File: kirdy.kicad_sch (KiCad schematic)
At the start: 0 parts

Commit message: add driver stage sch
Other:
- added sheet driveStage (driveStage.kicad_sch)
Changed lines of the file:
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@@
 (kicad_sch (version 20211123) (generator eeschema)
   (paper "A3")
-  (symbol_instances)
+  (sheet (at 270.51 93.98) (size 25.4 19.05) (fields_autoplaced)
+    (stroke (width 0.1524) (type solid) (color 0 0 0 0))
+    (fill (color 0 0 0 0.0000))
+    (property "Sheet name" "driveStage" (id 0) (at 270.51 93.2684 0)
+      (effects (font (size 1.27 1.27)) (justify left bottom))
+    )
+    (property "Sheet file" "driveStage.kicad_sch" (id 1) (at 270.51 113.6146 0)
+      (effects (font (size 1.27 1.27)) (justify left top))
+    )
+    (pin "GND_SEN" output (at 270.51 106.68 180)
+      (effects (font (size 1.27 1.27)) (justify left))
+    )
+    (pin "LD-" output (at 295.91 106.68 0)
+      (effects (font (size 1.27 1.27)) (justify right))
+    )
+    (pin "LD+" output (at 295.91 100.33 0)
+      (effects (font (size 1.27 1.27)) (justify right))
+    )
+    (pin "LD_DAC" input (at 270.51 100.33 180)
+      (effects (font (size 1.27 1.27)) (justify left))
+    )
+  )
+  (sheet_instances
+    (path "/" (page "1"))
+    (path "/7fc2620b-bac4-49c0-a276-7d2a46898037" (page "2"))
+  )
+  (symbol_instances
+    (path "/7fc2620b-bac4-49c0-a276-7d2a46898037/7f2ae8de-9741-4de8-8b3e-0cbf1d496d0b"
+      (reference "#PWR?") (unit 1) (value "GND") (footprint "")
+    )
+    (path "/7fc2620b-bac4-49c0-a276-7d2a46898037/89be3b87-0315-4e54-b96d-03ea2414961f"
+      (reference "#PWR?") (unit 1) (value "+9VA") (footprint "")
+    )
+    (path "/7fc2620b-bac4-49c0-a276-7d2a46898037/9119661d-44f6-446a-9801-ce7bdada5f6c"
+      (reference "#PWR?") (unit 1) (value "-6V") (footprint "")
+    )
+    (path "/7fc2620b-bac4-49c0-a276-7d2a46898037/91ab56d9-20e0-4249-9981-a5a11df12169"
+      (reference "#PWR?") (unit 1) (value "GND") (footprint "")
+    )
+    (path "/7fc2620b-bac4-49c0-a276-7d2a46898037/94d8c0ef-788e-401d-b84d-b1e1c20b5ad0"
+      (reference "#PWR?") (unit 1) (value "+15V") (footprint "")
+    )
+    (path "/7fc2620b-bac4-49c0-a276-7d2a46898037/b5336e6d-b40e-4302-8070-a2e20e788664"
+      (reference "#PWR?") (unit 1) (value "GND") (footprint "")
+    )
+    (path "/7fc2620b-bac4-49c0-a276-7d2a46898037/b9da8ef3-8685-462f-8a3e-c3779610dd6e"
+      (reference "#PWR?") (unit 1) (value "+9VA") (footprint "")
+    )
+    (path "/7fc2620b-bac4-49c0-a276-7d2a46898037/bcbda3c7-7e9b-441d-b86c-cb49c070efc8"
+      (reference "#PWR?") (unit 1) (value "GND") (footprint "")
+    )
+    (path "/7fc2620b-bac4-49c0-a276-7d2a46898037/c66bdd89-bde9-4c51-94d1-a5152521e393"
+      (reference "#PWR?") (unit 1) (value "+8V") (footprint "")
+    )
+    (path "/7fc2620b-bac4-49c0-a276-7d2a46898037/cc384f65-7f0d-4678-98b8-ac73a44b359a"
+      (reference "#PWR?") (unit 1) (value "-6V") (footprint "")
+    )
+    (path "/7fc2620b-bac4-49c0-a276-7d2a46898037/cee05324-592d-4982-97cf-77964e04d4ac"
+      (reference "#PWR?") (unit 1) (value "GND") (footprint "")
+    )
+    (path "/7fc2620b-bac4-49c0-a276-7d2a46898037/d79107b5-7dc2-415e-945e-ed09fd9cfe77"
+      (reference "#PWR?") (unit 1) (value "-6V") (footprint "")
+    )
+    (path "/7fc2620b-bac4-49c0-a276-7d2a46898037/e25c6fe0-b2f1-40d9-ac68-8d2d96853d01"
+      (reference "#PWR?") (unit 1) (value "+9VA") (footprint "")
+    )
+    (path "/7fc2620b-bac4-49c0-a276-7d2a46898037/e42d3e8b-b42d-4358-a3c4-e0df9650fb31"
+      (reference "#PWR?") (unit 1) (value "+9VA") (footprint "")
+    )
+    (path "/7fc2620b-bac4-49c0-a276-7d2a46898037/f4f71da4-602f-4bb4-aa0d-484f08abc473"
+      (reference "#PWR?") (unit 1) (value "+15V") (footprint "")
+    )
+    (path "/7fc2620b-bac4-49c0-a276-7d2a46898037/220f7c28-69b1-42e7-83ce-7bb31e5cf05d"
+      (reference "C?") (unit 1) (value "2u") (footprint "")
+    )
+    (path "/7fc2620b-bac4-49c0-a276-7d2a46898037/474c426e-35aa-4bc8-ac82-e7acb6bf064c"
+      (reference "C?") (unit 1) (value "10n") (footprint "")
+    )
+    (path "/7fc2620b-bac4-49c0-a276-7d2a46898037/e8a7395c-b328-4a48-81a4-7da6a4753156"
+      (reference "C?") (unit 1) (value "2u") (footprint "")
+    )
+    (path "/7fc2620b-bac4-49c0-a276-7d2a46898037/e2529b99-2d1f-424b-948b-cb83b5441da0"
+      (reference "D?") (unit 1) (value "AQ4020-01FTG-C") (footprint "")
+    )
+    (path "/7fc2620b-bac4-49c0-a276-7d2a46898037/fc3e1e88-39dd-4e44-9550-0de98037638f"
+      (reference "J?") (unit 1) (value "MOD_IN") (footprint "")
+    )
+    (path "/7fc2620b-bac4-49c0-a276-7d2a46898037/d481456c-376e-4c18-aab0-143380a08806"
+      (reference "Q?") (unit 1) (value "CSD17507Q5A") (footprint "Package_TO_SOT_SMD:TDSON-8-1")
+    )
+    (path "/7fc2620b-bac4-49c0-a276-7d2a46898037/066d5892-5cd5-4bea-b526-a87f3a5c11e8"
+      (reference "R?") (unit 1) (value "100") (footprint "")
+    )
+    (path "/7fc2620b-bac4-49c0-a276-7d2a46898037/3ee38521-8197-424b-afd0-d940f0fbf437"
+      (reference "R?") (unit 1) (value "100") (footprint "")
+    )
+    (path "/7fc2620b-bac4-49c0-a276-7d2a46898037/4f339c66-c682-43a9-8f4e-7ad41804bdc2"
+      (reference "R?") (unit 1) (value "300") (footprint "")
+    )
+    (path "/7fc2620b-bac4-49c0-a276-7d2a46898037/84d1caf1-6f0d-4adb-bda1-ca435ebeff03"
+      (reference "R?") (unit 1) (value "2k") (footprint "")
+    )
+    (path "/7fc2620b-bac4-49c0-a276-7d2a46898037/89ee40b5-e3cd-44df-ab7b-4cda054672f5"
+      (reference "R?") (unit 1) (value "R_Shunt") (footprint "")
+    )
+    (path "/7fc2620b-bac4-49c0-a276-7d2a46898037/affb61ec-84ab-440d-a648-f96126f479ed"
+      (reference "R?") (unit 1) (value "100") (footprint "")
+    )
+    (path "/7fc2620b-bac4-49c0-a276-7d2a46898037/b3c70cb7-9c59-476f-852d-2641f246969d"
+      (reference "R?") (unit 1) (value "50") (footprint "")
+    )
+    (path "/7fc2620b-bac4-49c0-a276-7d2a46898037/b999677c-fac2-421c-937e-afea837078d3"
+      (reference "R?") (unit 1) (value "100") (footprint "")
+    )
+    (path "/7fc2620b-bac4-49c0-a276-7d2a46898037/c5994ec4-b59b-4eb4-8847-d4ef36a60a0c"
+      (reference "R?") (unit 1) (value "1") (footprint "")
+    )
+    (path "/7fc2620b-bac4-49c0-a276-7d2a46898037/df19f4dc-6f09-439e-a4b3-58fc0b6e1223"
+      (reference "R?") (unit 1) (value "10") (footprint "")
+    )
+    (path "/7fc2620b-bac4-49c0-a276-7d2a46898037/6f857960-a9ff-452e-bba2-080502805e7a"
+      (reference "SW?") (unit 1) (value "SW_DIP_x03") (footprint "")
+    )
+    (path "/7fc2620b-bac4-49c0-a276-7d2a46898037/4553d9ae-3656-48c1-ba42-349c8ea6d675"
+      (reference "U?") (unit 1) (value "ADA4898-1YRDZ") (footprint "Package_SO:SOIC-8-1EP_3.9x4.9mm_P1.27mm_EP2.29x3mm")
+    )
+    (path "/7fc2620b-bac4-49c0-a276-7d2a46898037/75ce4c72-4d1d-4fd1-a700-9ce5fb7cb68a"
+      (reference "U?") (unit 1) (value "ADA4898-1YRDZ") (footprint "Package_SO:SOIC-8-1EP_3.9x4.9mm_P1.27mm_EP2.29x3mm")
+    )
+    (path "/7fc2620b-bac4-49c0-a276-7d2a46898037/cab8be84-b688-4aaa-b54c-d8be85dc55c5"
+      (reference "U?") (unit 1) (value "ADA4898-1YRDZ") (footprint "Package_SO:SOIC-8-1EP_3.9x4.9mm_P1.27mm_EP2.29x3mm")
+    )
+  )
 )

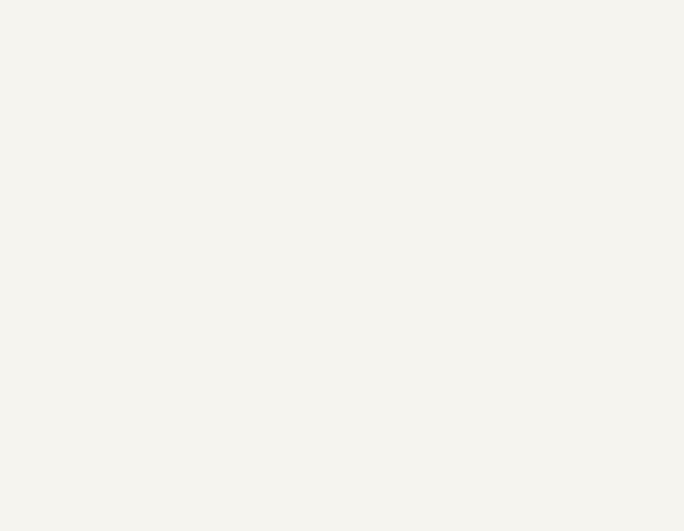
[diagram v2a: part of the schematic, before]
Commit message: add ref dac
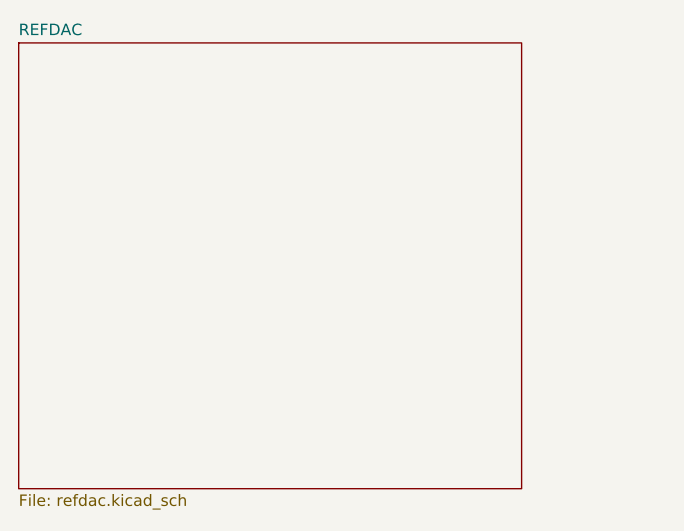
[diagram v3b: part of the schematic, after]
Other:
- added sheet REFDAC (refdac.kicad_sch)
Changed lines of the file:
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@@
 (kicad_sch (version 20211123) (generator eeschema)
   (paper "A3")
+  (sheet (at 173.99 91.44) (size 55.88 49.53) (fields_autoplaced)
+    (stroke (width 0.1524) (type solid) (color 0 0 0 0))
+    (fill (color 0 0 0 0.0000))
+    (property "Sheet name" "REFDAC" (id 0) (at 173.99 90.7284 0)
+      (effects (font (size 1.27 1.27)) (justify left bottom))
+    )
+    (property "Sheet file" "refdac.kicad_sch" (id 1) (at 173.99 141.5546 0)
+      (effects (font (size 1.27 1.27)) (justify left top))
+    )
+  )
   (sheet (at 270.51 93.98) (size 25.4 19.05) (fields_autoplaced)
     (stroke (width 0.1524) (type solid) (color 0 0 0 0))
@@
     (path "/" (page "1"))
     (path "/7fc2620b-bac4-49c0-a276-7d2a46898037" (page "2"))
+    (path "/5c501399-91aa-4646-9dc0-aa6b782690af" (page "3"))
   )
   (symbol_instances
+    (path "/7fc2620b-bac4-49c0-a276-7d2a46898037/22dd391c-8e48-413f-8e44-9f72eefb4601"
+      (reference "#PWR?") (unit 1) (value "+15V") (footprint "")
+    )
+    (path "/7fc2620b-bac4-49c0-a276-7d2a46898037/234258fd-ca43-4b0f-bd3b-37a0c1d653dc"
+      (reference "#PWR?") (unit 1) (value "+9VA") (footprint "")
+    )
+    (path "/7fc2620b-bac4-49c0-a276-7d2a46898037/30c37857-bcd7-4d18-b782-dd4e651118cd"
+      (reference "#PWR?") (unit 1) (value "-6V") (footprint "")
+    )
+    (path "/7fc2620b-bac4-49c0-a276-7d2a46898037/42e81420-64c1-4191-91f2-d9ce2b7f0c58"
+      (reference "#PWR?") (unit 1) (value "GND") (footprint "")
+    )
+    (path "/7fc2620b-bac4-49c0-a276-7d2a46898037/5f796a2f-98e9-46e3-a254-aaf7ea8e8609"
+      (reference "#PWR?") (unit 1) (value "+9VA") (footprint "")
+    )
+    (path "/7fc2620b-bac4-49c0-a276-7d2a46898037/692ead24-1a3f-435a-8011-daf8f013e94d"
+      (reference "#PWR?") (unit 1) (value "-6V") (footprint "")
+    )
+    (path "/7fc2620b-bac4-49c0-a276-7d2a46898037/799206b5-376e-4365-9dbe-4ba1050c7f50"
+      (reference "#PWR?") (unit 1) (value "GND") (footprint "")
+    )
     (path "/7fc2620b-bac4-49c0-a276-7d2a46898037/7f2ae8de-9741-4de8-8b3e-0cbf1d496d0b"
       (reference "#PWR?") (unit 1) (value "GND") (footprint "")
@@
       (reference "#PWR?") (unit 1) (value "+15V") (footprint "")
     )
+    (path "/7fc2620b-bac4-49c0-a276-7d2a46898037/95044b80-4a7b-44f0-ba10-b3f8d39e8d8b"
+      (reference "#PWR?") (unit 1) (value "GND") (footprint "")
+    )
     (path "/7fc2620b-bac4-49c0-a276-7d2a46898037/b5336e6d-b40e-4302-8070-a2e20e788664"
       (reference "#PWR?") (unit 1) (value "GND") (footprint "")
@@
       (reference "#PWR?") (unit 1) (value "-6V") (footprint "")
     )
+    (path "/7fc2620b-bac4-49c0-a276-7d2a46898037/e03d4cfa-81b2-4add-b063-90058145447f"
+      (reference "#PWR?") (unit 1) (value "-6V") (footprint "")
+    )
     (path "/7fc2620b-bac4-49c0-a276-7d2a46898037/e25c6fe0-b2f1-40d9-ac68-8d2d96853d01"
       (reference "#PWR?") (unit 1) (value "+9VA") (footprint "")
@@
       (reference "C?") (unit 1) (value "2u") (footprint "")
     )
+    (path "/7fc2620b-bac4-49c0-a276-7d2a46898037/39400eb9-6410-4341-8c26-1e54fd41195f"
+      (reference "C?") (unit 1) (value "10u") (footprint "")
+    )
     (path "/7fc2620b-bac4-49c0-a276-7d2a46898037/474c426e-35aa-4bc8-ac82-e7acb6bf064c"
       (reference "C?") (unit 1) (value "10n") (footprint "")
     )
+    (path "/7fc2620b-bac4-49c0-a276-7d2a46898037/6515a0cc-09fd-42e3-8559-ed97c2e10919"
+      (reference "C?") (unit 1) (value "100n") (footprint "")
+    )
+    (path "/7fc2620b-bac4-49c0-a276-7d2a46898037/7d6a0bc2-603a-43a2-992b-4f35cbb0a1f8"
+      (reference "C?") (unit 1) (value "100n") (footprint "")
+    )
+    (path "/7fc2620b-bac4-49c0-a276-7d2a46898037/9e5b3b75-838d-49ca-9d77-cb76ab7d1e4e"
+      (reference "C?") (unit 1) (value "10u") (footprint "")
+    )
+    (path "/7fc2620b-bac4-49c0-a276-7d2a46898037/cf733f3d-f3a4-44f4-a550-52da39242bf1"
+      (reference "C?") (unit 1) (value "100n") (footprint "")
+    )
+    (path "/7fc2620b-bac4-49c0-a276-7d2a46898037/e436bca2-7176-45a0-a972-406de4b69486"
+      (reference "C?") (unit 1) (value "100n") (footprint "")
+    )
     (path "/7fc2620b-bac4-49c0-a276-7d2a46898037/e8a7395c-b328-4a48-81a4-7da6a4753156"
       (reference "C?") (unit 1) (value "2u") (footprint "")
     )
+    (path "/7fc2620b-bac4-49c0-a276-7d2a46898037/f89d2343-5bb4-4a92-9abf-ee1606dfe7e0"
+      (reference "C?") (unit 1) (value "100n") (footprint "")
+    )
+    (path "/7fc2620b-bac4-49c0-a276-7d2a46898037/fdcb157d-2866-4fb4-853a-a66bf3c04c03"
+      (reference "C?") (unit 1) (value "100n") (footprint "")
+    )
     (path "/7fc2620b-bac4-49c0-a276-7d2a46898037/e2529b99-2d1f-424b-948b-cb83b5441da0"
       (reference "D?") (unit 1) (value "AQ4020-01FTG-C") (footprint "")
@@
     )
     (path "/7fc2620b-bac4-49c0-a276-7d2a46898037/89ee40b5-e3cd-44df-ab7b-4cda054672f5"
-      (reference "R?") (unit 1) (value "R_Shunt") (footprint "")
+      (reference "R?") (unit 1) (value "10") (footprint "")
     )
     (path "/7fc2620b-bac4-49c0-a276-7d2a46898037/affb61ec-84ab-440d-a648-f96126f479ed"
@@
       (reference "U?") (unit 1) (value "ADA4898-1YRDZ") (footprint "Package_SO:SOIC-8-1EP_3.9x4.9mm_P1.27mm_EP2.29x3mm")
     )
+    (path "/5c501399-91aa-4646-9dc0-aa6b782690af/5313797e-f430-448f-a9de-950ee2d2c9b9"
+      (reference "U?") (unit 1) (value "MAX5719xSD") (footprint "Package_SO:SOIC-14_3.9x8.7mm_P1.27mm")
+    )
     (path "/7fc2620b-bac4-49c0-a276-7d2a46898037/75ce4c72-4d1d-4fd1-a700-9ce5fb7cb68a"
       (reference "U?") (unit 1) (value "ADA4898-1YRDZ") (footprint "Package_SO:SOIC-8-1EP_3.9x4.9mm_P1.27mm_EP2.29x3mm")
@@
       (reference "U?") (unit 1) (value "ADA4898-1YRDZ") (footprint "Package_SO:SOIC-8-1EP_3.9x4.9mm_P1.27mm_EP2.29x3mm")
     )
-  )
+    (path "/5c501399-91aa-4646-9dc0-aa6b782690af/d75907ee-2f25-4b08-9fbe-327f008b7cae"
+      (reference "U?") (unit 1) (value "LTC6655BHLS8-4.096") (footprint "kirdy:LCC127P500X500X155-8N")
+    )
+  )
